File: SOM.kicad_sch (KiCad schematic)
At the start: 2 parts, among them J1 REF-226081-01, J2 REF-226081-01

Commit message: finished SOM 5V power, migrated altium stuff, finished pin study, added USB PHY (revise HS capability)
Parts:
- added JP2: BM1, symbol Jumper:SolderJumper_2_Bridged
- added JP3: BM2, symbol Jumper:SolderJumper_2_Open
- added JP4: BM0, symbol Jumper:SolderJumper_2_Bridged
- added JP5: BM3, symbol Jumper:SolderJumper_2_Bridged
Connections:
- net GND: now also J2.A01, J2.A02, J2.A05, J2.A06, J2.A09, J2.A10, J2.A13, J2.A16, J2.A19, J2.A22, J2.A25, J2.A28, J2.A31, J2.A34, J2.A37, J2.A40, J2.A43, J2.A45, J2.A49, J2.A53, J2.A57, J2.B03, J2.B04, J2.B07, J2.B08, J2.B11, J2.B14, J2.B17, J2.B20, J2.B23, J2.B26, J2.B29, J2.B32, J2.B35, J2.B38, J2.B41, J2.B43, J2.B47, J2.B51, J2.B55, J2.C01, J2.C02, J2.C05, J2.C06, J2.C09, J2.C10, J2.C13, J2.C16, J2.C19, J2.C22, J2.C25, J2.C28, J2.C31, J2.C34, J2.C37, J2.C40, J2.C43, J2.C45, J2.C49, J2.C53, J2.C57, J2.D03, J2.D04, J2.D07, J2.D08, J2.D11, J2.D14, J2.D17, J2.D20, J2.D23, J2.D26, J2.D29, J2.D32, J2.D35, J2.D38, J2.D41, J2.D43, J2.D47, J2.D51, J2.D55, JP2.1 (A), JP3.1 (A), JP4.1 (A), JP5.1 (A)
- net VDD_HPC: now reaches J2.C44
- net VDD_HPC: now also J2.D42
- net VDD_HDC: now reaches J2.D59
- net VDD_HDC: now also J2.D60
- net VDD_HPB: now reaches J2.A44
- net VDD_HPB: now also J2.B42
- net VDD_HDB: now reaches J2.B59
- net VDD_HDB: now also J2.B60
- net VDD_HPA: now reaches J1.D01
- net VDD_HPA: now also J1.D02
- net HPA6_P: now reaches J1.A03
- net HPA6_N: now reaches J1.A04
- net HPA_CLK0_P: now reaches J1.A06
- net HPA_CLK0_N: now reaches J1.A07
- net HPA12_P: now reaches J1.A09
- net HPA12_N: now reaches J1.A10
- net HPA13_P: now reaches J1.A12
- net HPA13_N: now reaches J1.A13
- net HDA9: now reaches J1.A15
- net HDA10: now reaches J1.A16
- net HDA11: now reaches J1.A17
- net BOOT_MODE0: now reaches J1.A27
- net BOOT_MODE0: now also JP4.2 (B)
- net BOOT_MODE1: now reaches J1.A28
- net BOOT_MODE1: now also JP2.2 (B)
- net BOOT_MODE2: now reaches J1.A29
- net BOOT_MODE2: now also JP3.2 (B)
- net BOOT_MODE3: now reaches J1.A30
- net BOOT_MODE3: now also JP5.2 (B)
- net VDD_HDA: now reaches J1.B13
- net VDD_HDA: now also J1.B14
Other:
- note added: "SOM240_2"
- note removed: ""MODE" pins are to select boot mode check the datasheet and add the table here reference design has a 470R pulldown on each"
- moved on the sheet: J1B, J2B

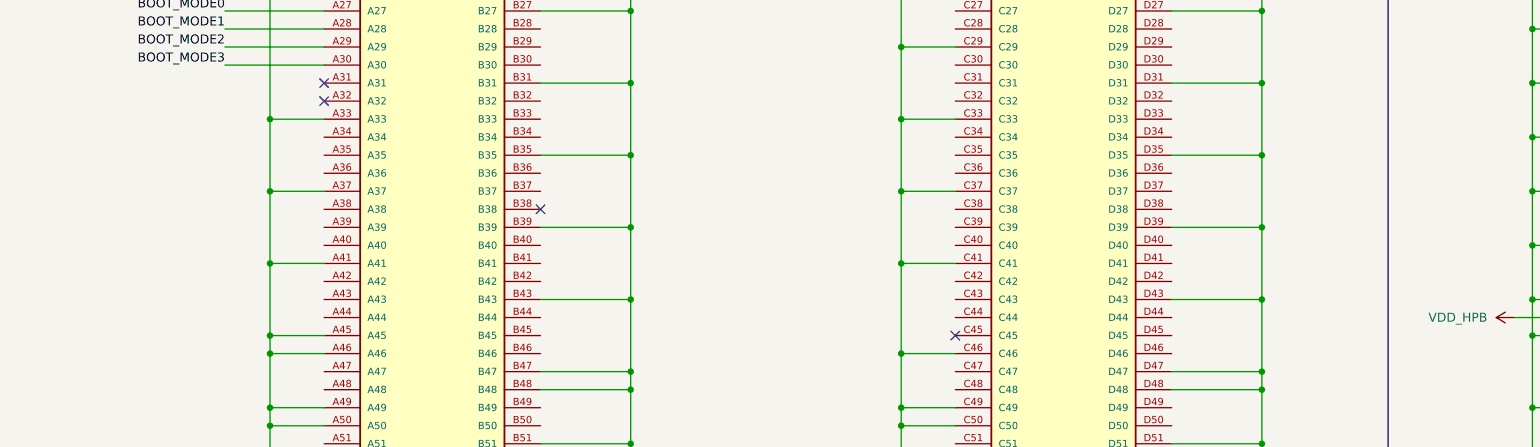
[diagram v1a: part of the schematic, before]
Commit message: added USB (needs revision), fixed medium voltage rail
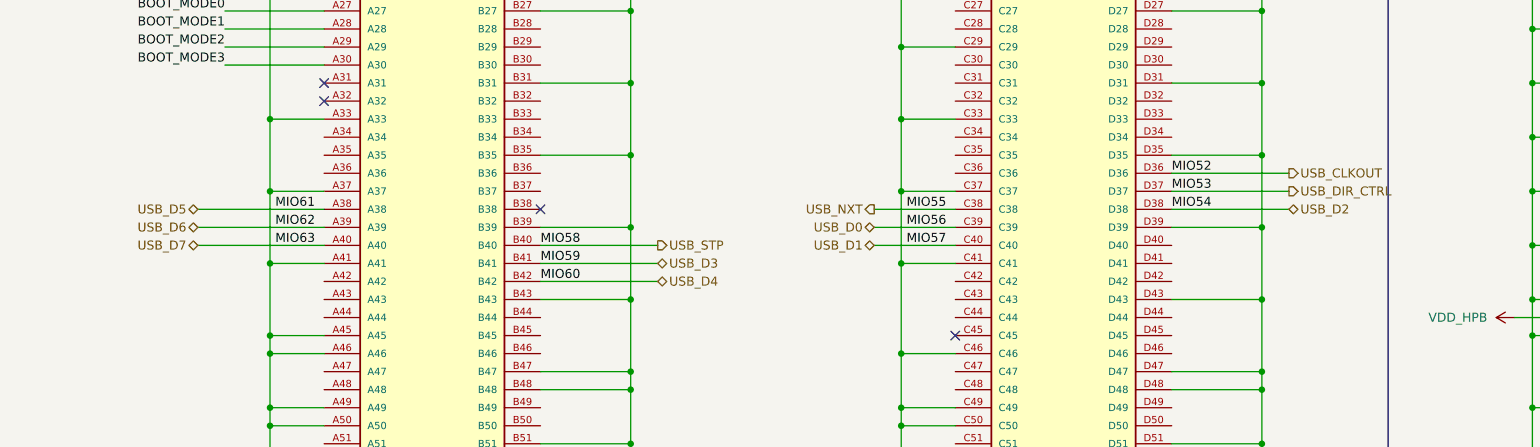
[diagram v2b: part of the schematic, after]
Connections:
- net USB_NXT: now reaches J1.C38
- net USB_D0: now reaches J1.C39
- net USB_D1: now reaches J1.C40
- net USB_CLKOUT: now reaches J1.D36
- net USB_DIR_CTRL: now reaches J1.D37
- net USB_D2: now reaches J1.D38
- net USB_D5: now reaches J1.A38
- net USB_D6: now reaches J1.A39
- net USB_D7: now reaches J1.A40
- net USB_STP: now reaches J1.B40
- net USB_D3: now reaches J1.B41
- net USB_D4: now reaches J1.B42

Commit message: almost finished, phew! just dd +/- 5v rails, connect the SDIO & power enable pins and figure out the rest of the clocking chain
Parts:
- added C133, C137, C142, C143, C147, C148, C150, C151, C154, C155: 100nF, symbol Device:C
- added C134, C138: 1uF, symbol Device:C
- added C135, C136, C139, C140: 47uF, symbol Device:C
- added C141, C144, C149, C152: 4.7uF, symbol Device:C
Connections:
- net VCCOEN_PS_M2C is gone; now on net SOM_PS_PWR_EN: J1.A19
- net GND: now also C133.2, C134.2, C135.2, C136.2, C137.2, C138.2, C139.2, C140.2, C141.2, C142.2, C143.2, C144.2, C147.2, C148.2, C149.2, C150.2, C151.2, C152.2, C154.2, C155.2
- net VCC_SOM: now also C133.1, C134.1, C135.1, C136.1, C137.1, C138.1, C139.1, C140.1
- net VDD_HDA: now also C141.1, C142.1, C143.1
- net VDD_HDB: now also C149.1, C150.1, C151.1
- net VDD_HDC: now also C144.1, C147.1, C148.1
- net VDD_HPA: now also C152.1, C154.1, C155.1
- net AFE_OUTPUTS27: now reaches J2.C46
- net AFE_OUTPUTS28: now reaches J2.C47
- net AFE_OUTPUTS29: now reaches J2.C48
- net AFE_OUTPUTS33: now reaches J2.C50
- net AFE_OUTPUTS34: now reaches J2.C51
- net AFE_OUTPUTS35: now reaches J2.C52
- net AFE_OUTPUTS39: now reaches J2.C54
- net AFE_OUTPUTS40: now reaches J2.C55
- net AFE_OUTPUTS41: now reaches J2.C56
- net AFE_OUTPUTS45: now reaches J2.C58
- net AFE_OUTPUTS46: now reaches J2.C59
- net AFE_OUTPUTS47: now reaches J2.C60
- net AFE_OUTPUTS24: now reaches J2.D44
- net AFE_OUTPUTS25: now reaches J2.D45
- net AFE_OUTPUTS26: now reaches J2.D46
- net AFE_OUTPUTS30: now reaches J2.D48
- net AFE_OUTPUTS31: now reaches J2.D49
- net AFE_OUTPUTS32: now reaches J2.D50
- net AFE_OUTPUTS36: now reaches J2.D52
- net AFE_OUTPUTS37: now reaches J2.D53
- net AFE_OUTPUTS38: now reaches J2.D54
- net AFE_OUTPUTS42: now reaches J2.D56
- net AFE_OUTPUTS43: now reaches J2.D57
- net AFE_OUTPUTS44: now reaches J2.D58
- net AFE_OUTPUTS3: now reaches J2.A46
- net AFE_OUTPUTS4: now reaches J2.A47
- net AFE_OUTPUTS5: now reaches J2.A48
- net AFE_OUTPUTS9: now reaches J2.A50
- net AFE_OUTPUTS10: now reaches J2.A51
- net AFE_OUTPUTS11: now reaches J2.A52
- net AFE_OUTPUTS15: now reaches J2.A54
- net AFE_OUTPUTS16: now reaches J2.A55
- net AFE_OUTPUTS17: now reaches J2.A56
- net AFE_OUTPUTS21: now reaches J2.A58
- net AFE_OUTPUTS22: now reaches J2.A59
- net AFE_OUTPUTS23: now reaches J2.A60
- net AFE_OUTPUTS0: now reaches J2.B44
- net AFE_OUTPUTS1: now reaches J2.B45
- net AFE_OUTPUTS2: now reaches J2.B46
- net AFE_OUTPUTS6: now reaches J2.B48
- net AFE_OUTPUTS7: now reaches J2.B49
- net AFE_OUTPUTS8: now reaches J2.B50
- net AFE_OUTPUTS12: now reaches J2.B52
- net AFE_OUTPUTS13: now reaches J2.B53
- net AFE_OUTPUTS14: now reaches J2.B54
- net AFE_OUTPUTS18: now reaches J2.B56
- net AFE_OUTPUTS19: now reaches J2.B57
- net AFE_OUTPUTS20: now reaches J2.B58
- net SOM_SYNC_CLK_P: now reaches J1.C03
- net SOM_SYNC_CLK_N: now reaches J1.C04
- net AFE3_CSn: now reaches J1.C18
- net AFE3_MUXA: now reaches J1.C19
- net AFE3_AUX: now reaches J1.C20
- net AFE4_DSYNC: now reaches J1.C22
- net AFE4_CSn: now reaches J1.C23
- net AFE4_MUXA: now reaches J1.C24
- net PULSER_TSHUT: now reaches J1.C30
- net SOM_5V_PG: now reaches J1.C31
- net PULSER_WAKEUP: now reaches J1.C34
- net PULSER_RESET: now reaches J1.C35
- net PULSER_CRC_ERR: now reaches J1.C36
- net AFE_SCLK: now reaches J1.D16
- net AFE4_AUX: now reaches J1.D17
- net AFE_SDIO: now reaches J1.D18
- net 50V_EN: now reaches J1.A34
- net 100V_EN: now reaches J1.A35
- net SOM_PS_PWR_EN: now reaches J1.A36
- net PULSER_BF_SYNC_CLK_P: now reaches J1.B01
- net PULSER_BF_SYNC_CLK_N: now reaches J1.B02
- net PULSER_SPI_CS0: now reaches J1.B04
- net PULSER_SPI_CS1: now reaches J1.B05
- net AFE1_AUX: now reaches J1.B16
- net AFE2_DSYNC: now reaches J1.B17
- net AFE2_CSn: now reaches J1.B18
- net AFE2_MUXA: now reaches J1.B20
- net AFE2_AUX: now reaches J1.B21
- net AFE3_DSYNC: now reaches J1.B22
- net PULSER_TXRX: now reaches J1.B29
- net PULSER_SPI_CRC_EN: now reaches J1.B30
- net PULSER_1V8_EN: now reaches J1.B32
- net CLK_PWR_EN: now reaches J1.B33
- net USB_1V8_EN: now reaches J1.B34
- net PULSER_SPI_SDOUT: now reaches J1.B36
- net PULSER_SPI_MODE: now reaches J1.B37
- net HDA10 renamed AFE1_CSn
- net HDA11 renamed AFE1_MUXA
- net HDA9 renamed AFE1_DSYNC
- net HPA12_N renamed PULSER_SPI_D1_N
- net HPA12_P renamed PULSER_SPI_D1_P
- net HPA13_N renamed PULSER_SPI_SE_N
- net HPA13_P renamed PULSER_SPI_SE_P
- net HPA6_N renamed PULSER_SPI_D0_N
- net HPA6_P renamed PULSER_SPI_D0_P
- net HPA_CLK0_N renamed PULSER_SPI_CLK_N
- net HPA_CLK0_P renamed PULSER_SPI_CLK_P
- net VCCOEN_PL_M2C renamed SOM_PL_PWR_EN
- no-connect marks 4 -> 6
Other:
- note added: "Bank 501"
- note added: "Bank 502"
- note added: "HDA"
- note added: "HDB"
- note added: "HDC"
- note added: "HPA"
- moved on the sheet: JP2, JP3, JP4, JP5

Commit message: DONE! hust needs a final revision, checking termination throughout the circuit and verifying the signal chain
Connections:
- net AFE1_1V8_EN: now also J1.A42
- net AFE1_3V3_EN: now also J1.A43
- net AFE2_1V8_EN: now also J1.A44
- net AFE2_3V3_EN: now also J1.B44
- net AFE3_1V8_EN: now also J1.B45
- net AFE3_3V3_EN: now also J1.B46
- net AFE4_1V8_EN: now also J1.C43
- net AFE4_3V3_EN: now also J1.C44
- net SD_CLK: now also J1.D33
- net SD_CMD: now also J1.D34
- net SD_DAT0: now also J1.D28
- net SD_DAT1: now also J1.D29
- net SD_DAT2: now also J1.D30
- net SD_DAT3: now also J1.D32
- net SD_DETECT: now also J1.D20
- net SD_3V3_EN: now reaches J1.C42
- net IM_5V_EN: now reaches J1.D44
- net -5V_EN: now reaches J1.D45
- no-connect marks 6 -> 40

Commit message: HDMI was requested so add it and give the signal chain a final revision
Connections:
- net EXT_INT1: now reaches J1.D21
- net EXT_INT2: now reaches J1.D22
- net EXT_RESET: now reaches J1.D40
- net EXT_AFE_CS1: now reaches J1.D41
- net EXT_AFE_CS2: now reaches J1.D42
- net AFE1_1V8_EN renamed AFE_1V8_EN
- net AFE1_3V3_EN renamed AFE_3V3_EN
- net AFE2_1V8_EN renamed CLK_1V8_EN
- net AFE2_3V3_EN renamed EXT_MISO
- net AFE3_1V8_EN renamed EXT_MOSI
- net AFE3_3V3_EN renamed EXT_SCLK
- net AFE4_1V8_EN renamed EXT_MUX_CS1
- net AFE4_3V3_EN renamed EXT_MUX_CS2
- net USB_CLKOUT renamed USB_RESET

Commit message: ALL IS DONE EXCEPT HDMI PLEASE HELP
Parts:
- added C262: 100nF, symbol Device:C
- added R108: 10K, symbol Device:R_US
- added SW1: RESET, Button_Switch_SMD:Nidec_Copal_CAS-120A, symbol Switch:SW_Push
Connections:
- net GND: now also C262.2, SW1.1
- net SD_3V3_EN: now also J1.A36; no longer J1.C42
- net SOM_PS_PWR_EN: no longer J1.A36
- net SOM_SYNC_CLK_N: now also J1.C13; no longer J1.C04
- net SOM_SYNC_CLK_P: now also J1.C12; no longer J1.C03
- net VCC_SOM: now also R108.1; no longer J1.A59, J1.A60, J1.B60, J1.C59, J1.C60, J1.D60
- net PWROFF_ C2M_L: now reaches J1.B26
- net PWROFF_ C2M_L: now also C262.1, R108.2, SW1.2
- new net SOM_5V: J1.A59, J1.A60, J1.B60, J1.C59, J1.C60, J1.D60
- new net USB_26MHZ: J1.C42
- no-connect marks 40 -> 39
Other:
- note added: "Reset Button"

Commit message: started layout, finished 90% of individual section placement, need to finish remaining and integrate together in PCB and apply schematic edits before
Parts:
- C501: renamed from C137; footprint (none) -> Capacitor_SMD:C_0402_1005Metric
- C502: renamed from C138; footprint (none) -> Capacitor_SMD:C_0402_1005Metric
- C503: renamed from C139; footprint (none) -> Capacitor_SMD:C_0805_2012Metric
- C504: renamed from C140; footprint (none) -> Capacitor_SMD:C_0805_2012Metric
- C505: renamed from C133; footprint (none) -> Capacitor_SMD:C_0402_1005Metric
- C506: renamed from C134; footprint (none) -> Capacitor_SMD:C_0402_1005Metric
- C507: renamed from C135; footprint (none) -> Capacitor_SMD:C_0805_2012Metric
- C508: renamed from C136; footprint (none) -> Capacitor_SMD:C_0805_2012Metric
- C509: renamed from C152; footprint (none) -> Capacitor_SMD:C_0805_2012Metric
- C510: renamed from C154; footprint (none) -> Capacitor_SMD:C_0402_1005Metric
- C511: renamed from C155; footprint (none) -> Capacitor_SMD:C_0402_1005Metric
- C512: renamed from C262; footprint (none) -> Capacitor_SMD:C_0402_1005Metric
- C513: renamed from C141; footprint (none) -> Capacitor_SMD:C_0805_2012Metric
- C514: renamed from C142; footprint (none) -> Capacitor_SMD:C_0402_1005Metric
- C515: renamed from C143; footprint (none) -> Capacitor_SMD:C_0402_1005Metric
- C516: renamed from C149; footprint (none) -> Capacitor_SMD:C_0805_2012Metric
- C517: renamed from C150; footprint (none) -> Capacitor_SMD:C_0402_1005Metric
- C518: renamed from C151; footprint (none) -> Capacitor_SMD:C_0402_1005Metric
- C519: renamed from C144; footprint (none) -> Capacitor_SMD:C_0805_2012Metric
- C520: renamed from C147; footprint (none) -> Capacitor_SMD:C_0402_1005Metric
- C521: renamed from C148; footprint (none) -> Capacitor_SMD:C_0402_1005Metric
- JP501: renamed from JP4; footprint (none) -> Jumper:SolderJumper-2_P1.3mm_Bridged_RoundedPad1.0x1.5mm
- JP502: renamed from JP2; footprint (none) -> Jumper:SolderJumper-2_P1.3mm_Bridged_RoundedPad1.0x1.5mm
- JP503: renamed from JP3; footprint (none) -> Jumper:SolderJumper-2_P1.3mm_Open_TrianglePad1.0x1.5mm
- JP504: renamed from JP5; footprint (none) -> Jumper:SolderJumper-2_P1.3mm_Bridged_RoundedPad1.0x1.5mm
- R501: renamed from R108; footprint (none) -> Resistor_SMD:R_0402_1005Metric
- renumbered J1 to J501, J2 to J502, SW1 to SW501
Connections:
- net CLK_1V8_EN is gone; now on net USB_1V8_EN: J501.A44
- net SOM_5V_PG is gone; now on net PULSER_TSHUT: J501.C31
- net PULSER_1V8_EN: now also J501.C30; no longer J501.B32
- net PULSER_TSHUT: no longer J501.C30
- net SOM_5V: now also C501.1, C502.1, C503.1, C504.1, C505.1, C506.1, C507.1, C508.1
- net USB_1V8_EN: no longer J501.B34
- net VCC_SOM: no longer C501.1, C502.1, C503.1, C504.1, C505.1, C506.1, C507.1, C508.1
- net CLK_PWR_EN renamed LCD_TX_MAIN
- new net LCD_POWER: J501.B32
- new net LCD_RX_MAIN: J501.B34
